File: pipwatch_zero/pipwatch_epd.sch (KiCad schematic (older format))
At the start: 16 parts, among them Q301 Si1304BDL, X301 MOLEX_FPC_RCPT_24POS

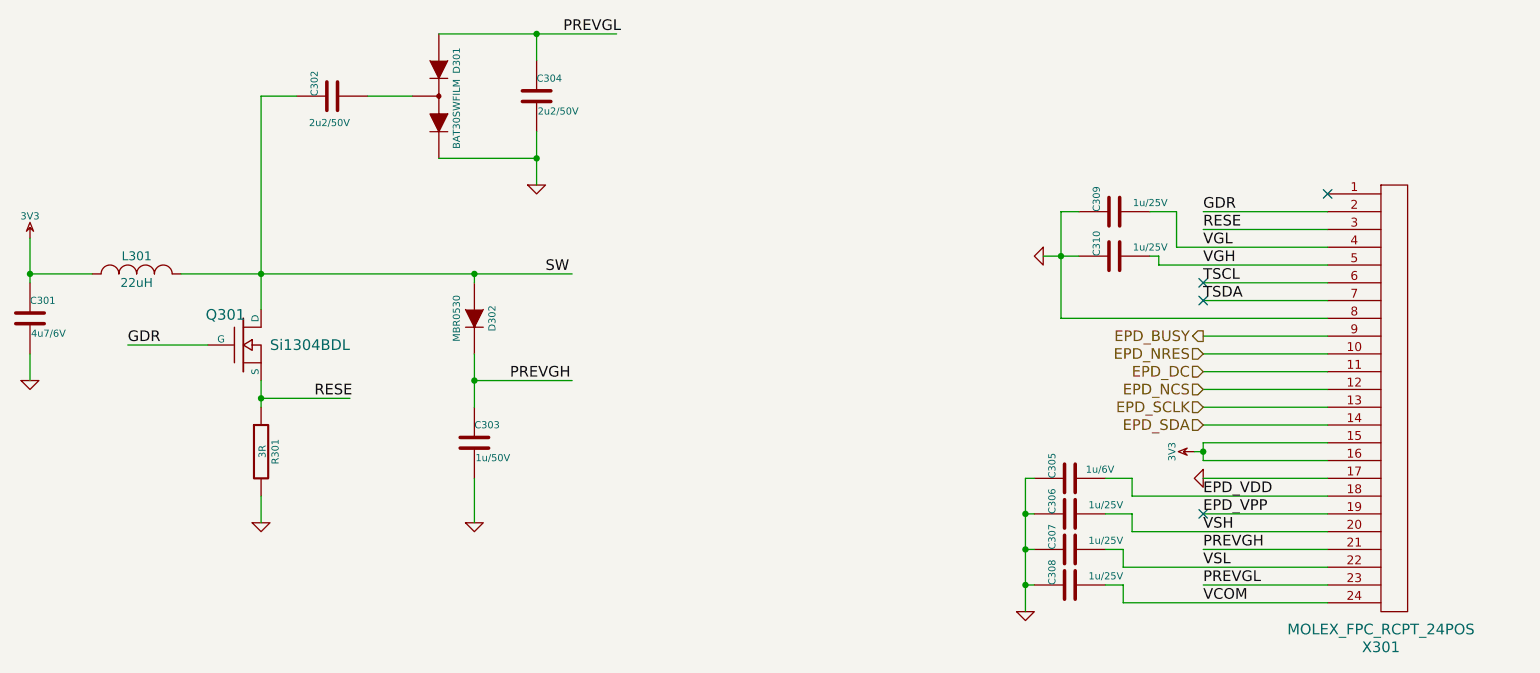
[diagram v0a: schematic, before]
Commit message: pipwatch_zero: footprints
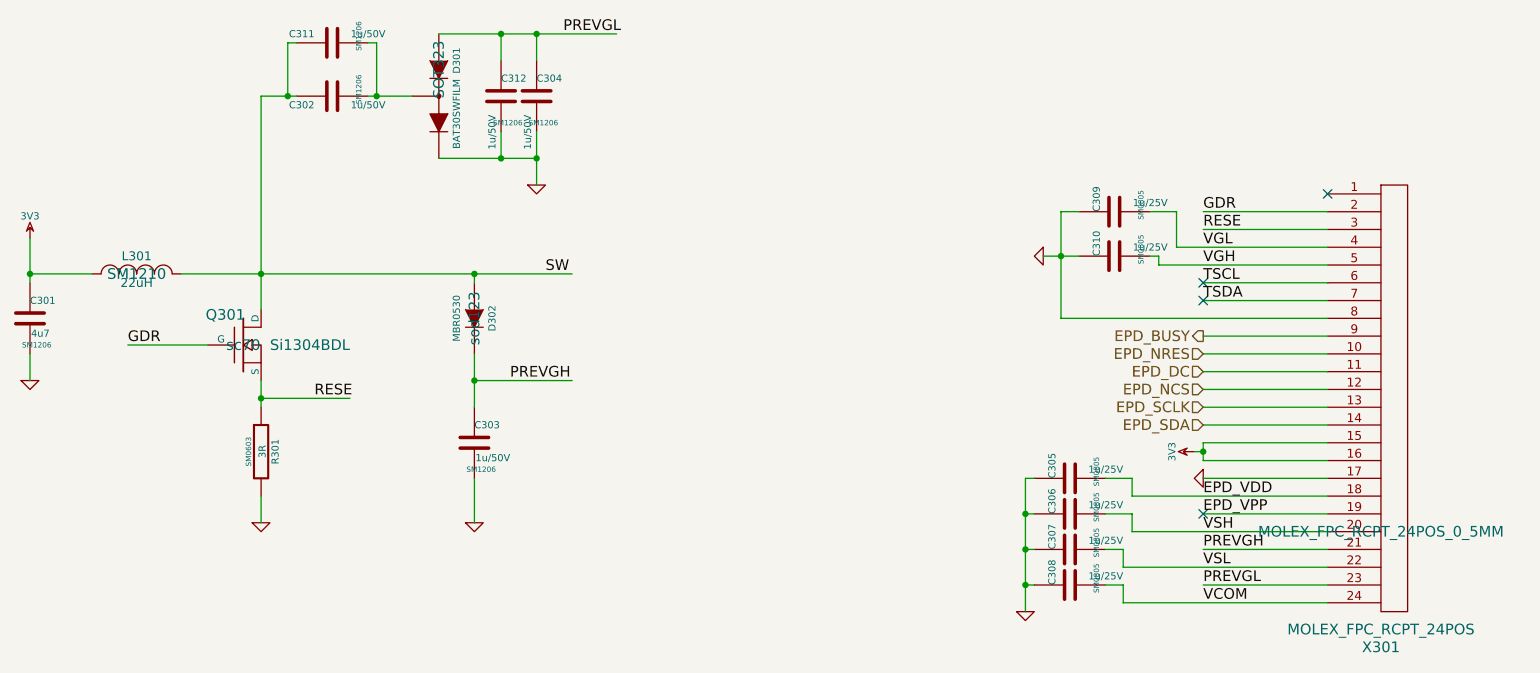
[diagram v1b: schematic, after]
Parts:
- added C311, C312: 1u/50V, SM1206, symbol C
- C301: value 4u7/6V -> 4u7; footprint (none) -> SM1206
- C302, C304: value 2u2/50V -> 1u/50V; footprint (none) -> SM1206
- C303: footprint (none) -> SM1206
- C305: value 1u/6V -> 1u/25V; footprint (none) -> SM0805
- C306, C307, C308, C309, C310: footprint ~ -> SM0805
- D301: footprint ~ -> SOT323
- D302: footprint ~ -> sod123
- L301: footprint ~ -> SM1210
- Q301: footprint ~ -> sc70
- R301: footprint ~ -> SM0603
- X301: footprint (none) -> MOLEX_FPC_RCPT_24POS_0_5MM
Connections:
- wire segments 64 -> 70
